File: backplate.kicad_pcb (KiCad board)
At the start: 2 copper layers, 43 x 43 mm, 1 part

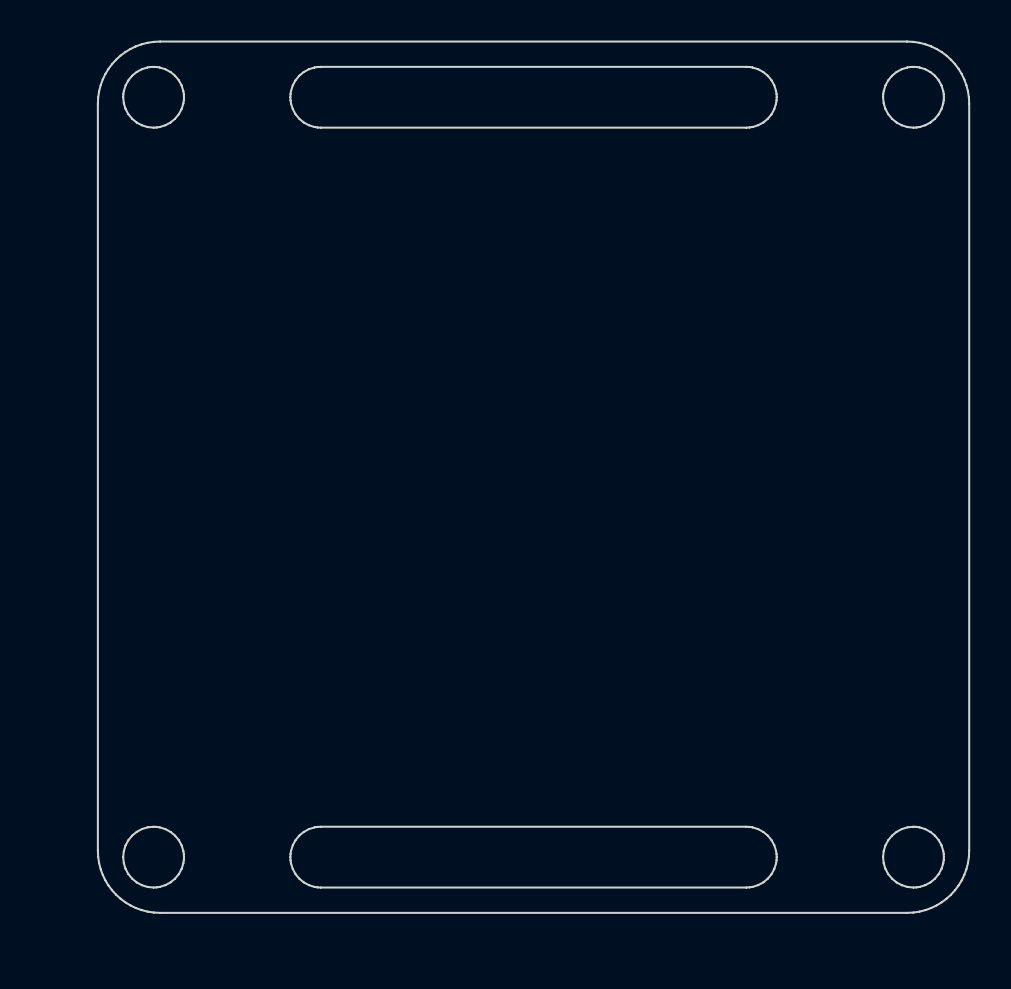
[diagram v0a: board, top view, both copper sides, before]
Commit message: update logos
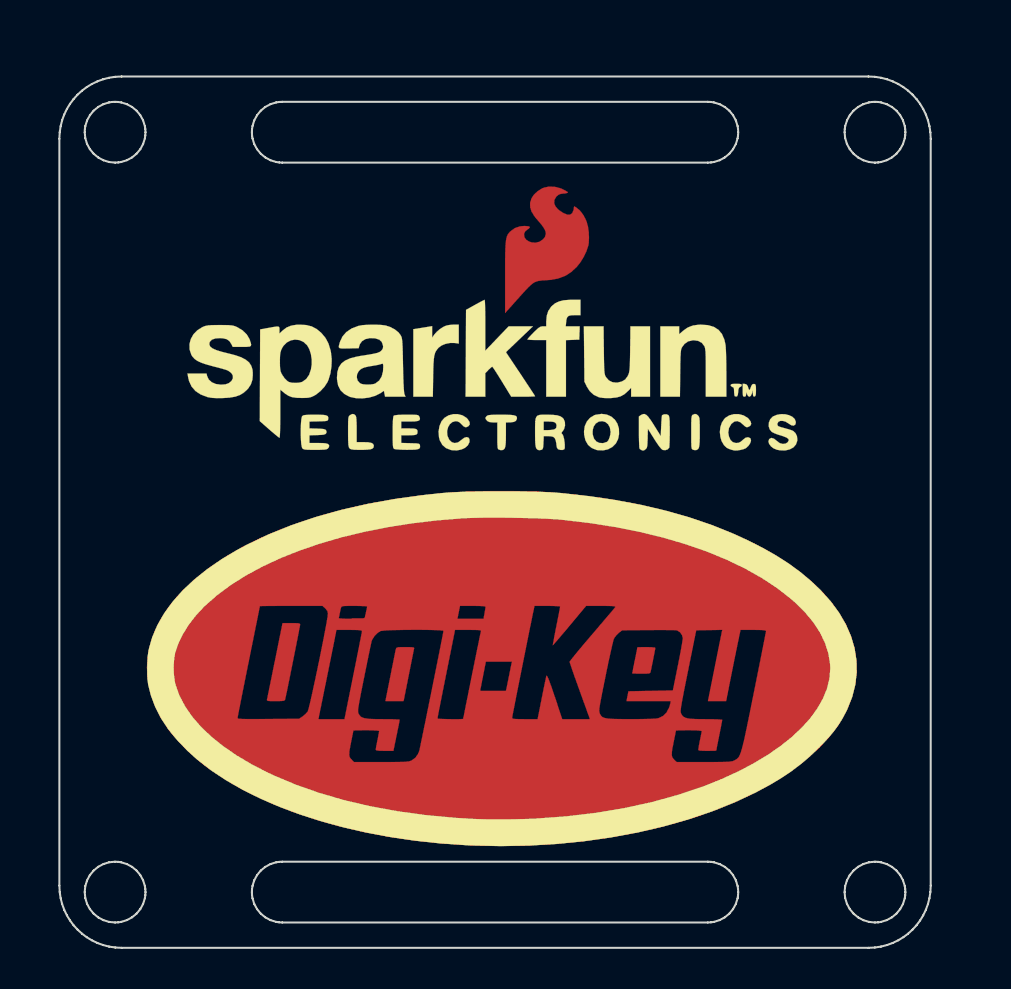
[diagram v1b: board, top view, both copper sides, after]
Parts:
- added Ref**: Val**, Badge-PCB:Sparkfun_logo, F.Cu at (107.8, 97.7)
- added Ref**: Val**, Badge-PCB:digikey_logo, F.Cu at (106.2, 110.0)
- moved Ref** 2.57 mm to (127.7, 105.3)

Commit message: combined artwork FP, updated PCB
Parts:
- removed the Ref** at (107.8, 97.7)
- removed the Ref** at (106.2, 110.0)
- added Ref**: Val**, Badge-PCB:combined, F.Cu at (104.9, 105.0)
- added Ref**: Val**, Badge-PCB:oshw-us000214, F.Cu at (103.8, 104.5)
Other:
- board text added: "Designed by: Alex Camilo Michael Welling"
- board text added: "Sponsored by: Digi-Key, Sparkfun and OSHPark"

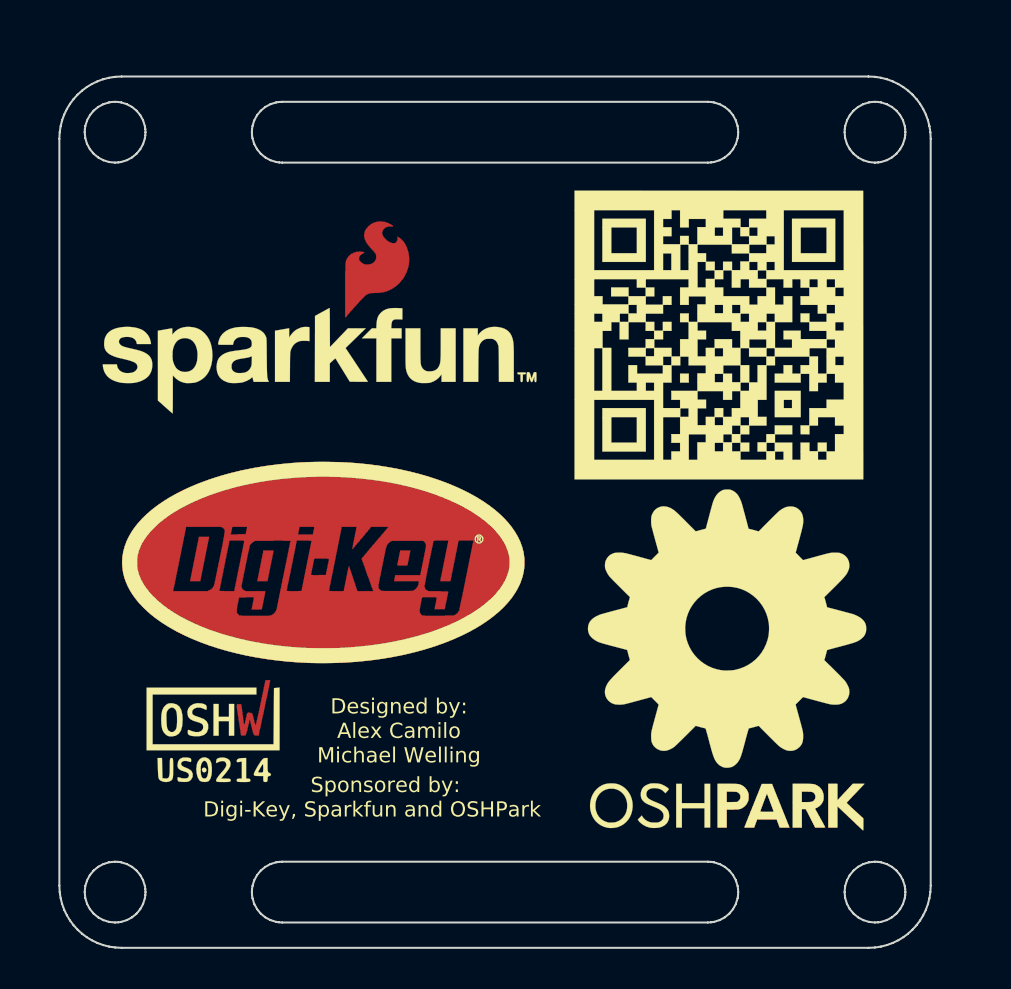
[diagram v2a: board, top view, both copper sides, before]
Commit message: update text on backplate
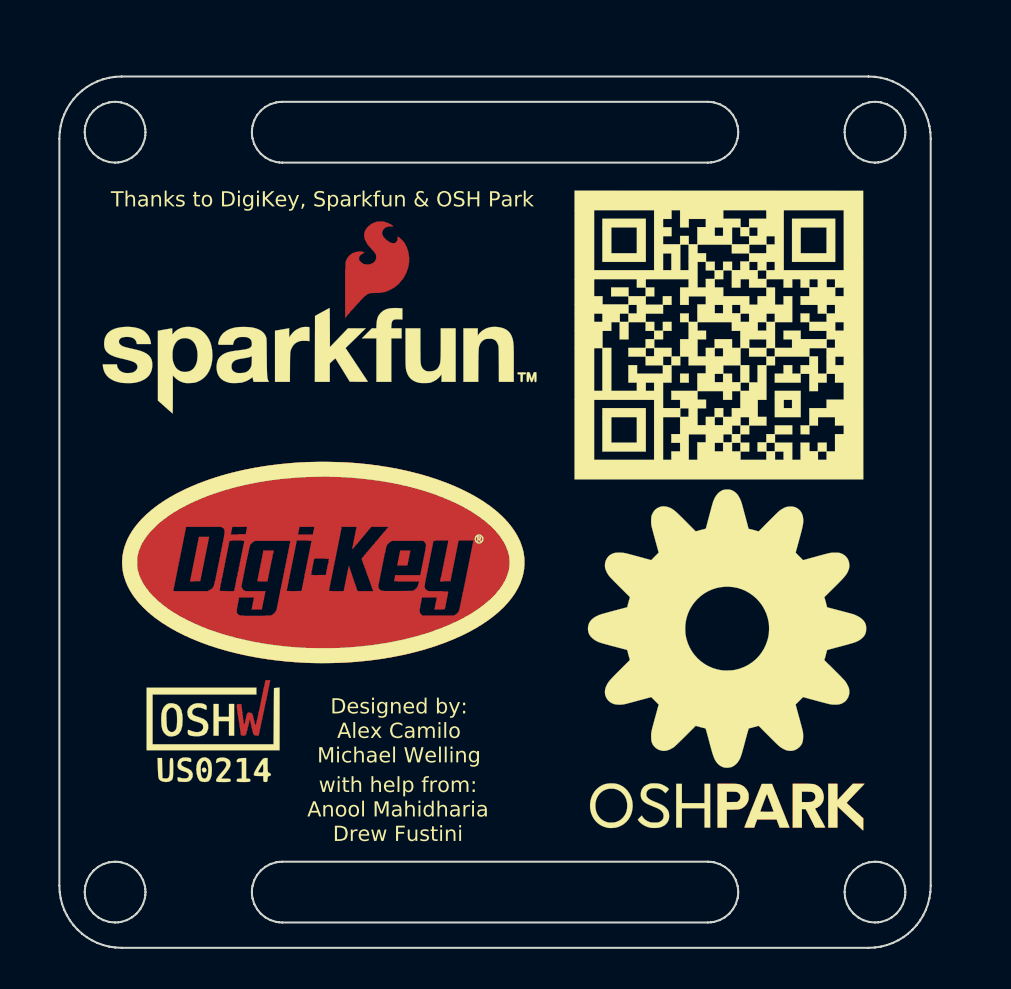
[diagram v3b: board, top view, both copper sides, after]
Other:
- board text added: "Thanks to DigiKey, Sparkfun & OSH Park"
- board text added: "with help from: Anool Mahidharia Drew Fustini"
- board text removed: "Sponsored by: Digi-Key, Sparkfun and OSHPark"
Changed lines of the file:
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@@
-(kicad_pcb (version 20171130) (host pcbnew 5.1.5-52549c5~84~ubuntu18.04.1)
+(kicad_pcb (version 20171130) (host pcbnew 5.1.5-52549c5~84~ubuntu19.04.1)
   (general
     (thickness 1.6)
-    (drawings 3)
+    (drawings 4)
     (tracks 0)
     (zones 0)
@@
       (xy -9.091094 6.570498)) (layer F.Cu) (width 0.01))
   )
-  (gr_text "    Sponsored by:\nDigi-Key, Sparkfun and OSHPark" (at 99.725 116.825) (layer F.SilkS)
+  (gr_text "with help from:\nAnool Mahidharia\nDrew Fustini" (at 100.99802 117.42674) (layer F.SilkS)
     (effects (font (size 0.75 0.75) (thickness 0.1)))
   )
+  (gr_text "Thanks to DigiKey, Sparkfun & OSH Park" (at 97.27184 87.32012) (layer F.SilkS)
+    (effects (font (size 0.75 0.75) (thickness 0.1)))
+  )

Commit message: add CircuitPython logo and tweak backplate artwork
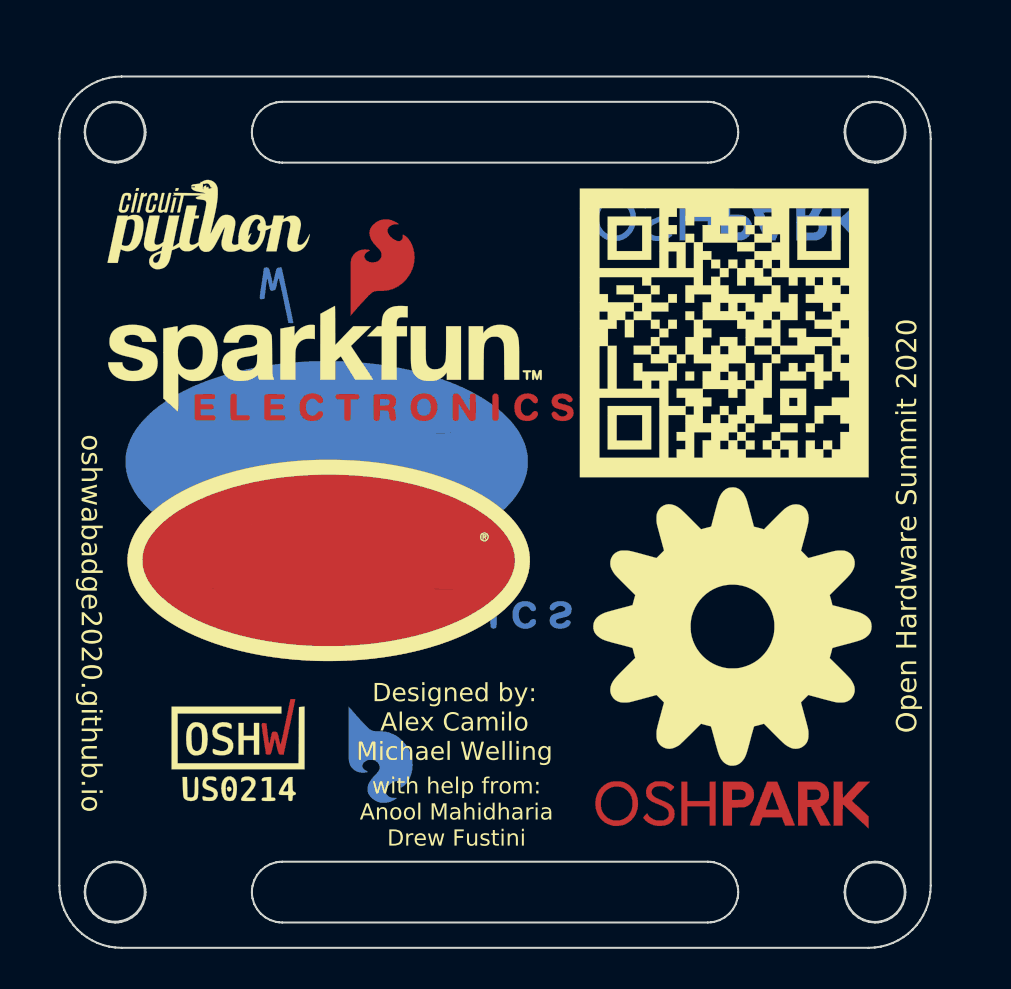
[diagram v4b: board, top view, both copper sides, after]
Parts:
- removed the Ref** at (104.9, 105.0)
- removed the Ref** at (103.8, 104.5)
- added REF**: M3, Badge-PCB:M3, F.Cu at (87.0, 121.5)
- added REF**: M3, Badge-PCB:M3, F.Cu at (124.5, 121.5)
- added REF**: M3, Badge-PCB:M3, F.Cu at (124.5, 84.0)
- added REF**: M3, Badge-PCB:M3, F.Cu at (87.0, 84.0)
- added Ref**: Val**, Badge-PCB:adafruit_circuit_python, B.Cu at (91.3, 116.3)
- added Ref**: Val**, Badge-PCB:combined-fixed, B.Cu at (105.1, 100.5)
- added Ref**: Val**, Badge-PCB:oshw-us000214, B.Cu at (93.1, 91.3)
- added Ref**: Val**, Badge-PCB:oshw-us000214, F.Cu at (93.2, 114.1)
- added Ref**: Val**, Badge-PCB:adafruit_circuit_python, F.Cu at (91.4, 89.2)
- added Ref**: Val**, Badge-PCB:combined-fixed, F.Cu at (105.2, 104.9)
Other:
- board text added: "Open Hardware Summit 2020"
- board text added: "oshwabadge2020.github.io"
- board text removed: "Thanks to DigiKey, Sparkfun & OSH Park"

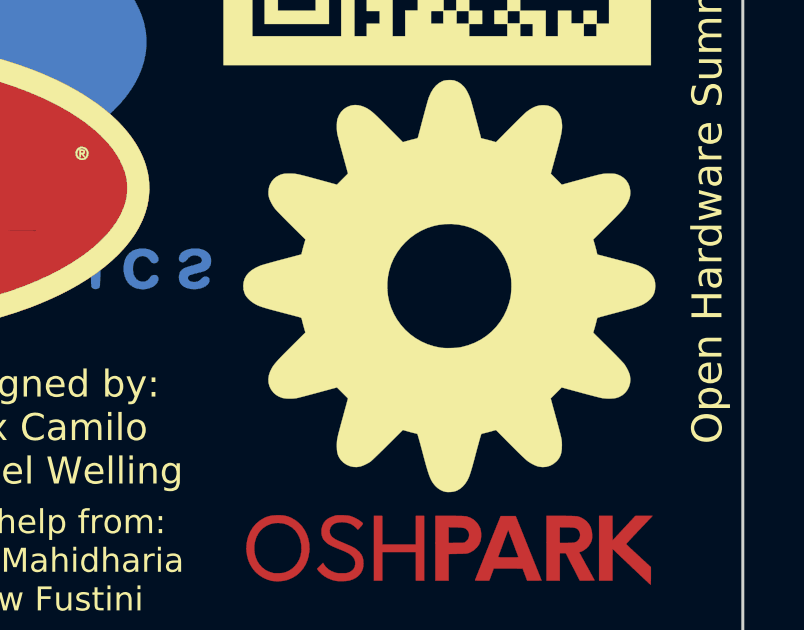
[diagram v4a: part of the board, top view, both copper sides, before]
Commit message: replace QR code on the backside of PCB
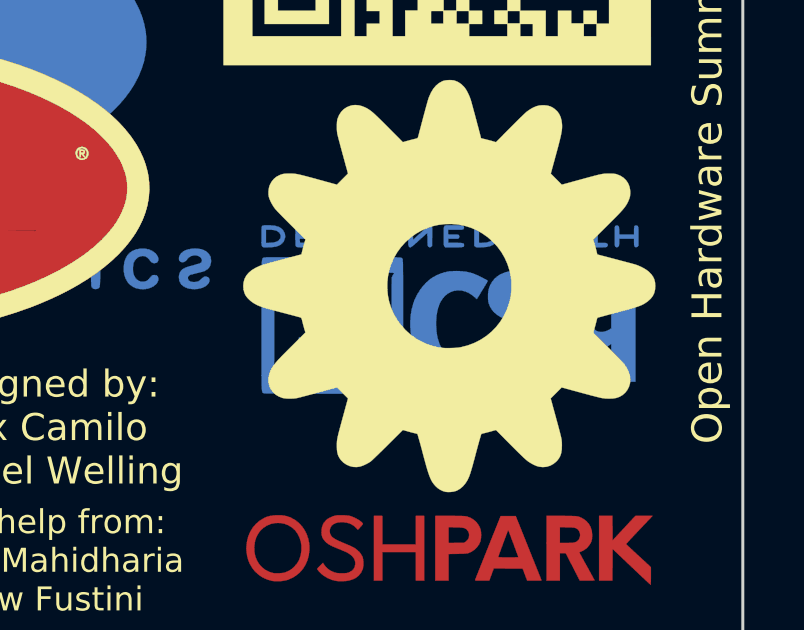
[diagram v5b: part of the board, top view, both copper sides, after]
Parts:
- added REF**: KiCad-Logo2_5mm_Copper, Symbol:KiCad-Logo2_5mm_Copper, B.Cu at (117.5, 109.4)
- moved Ref** 25.9 mm to (117.2, 115.1)
